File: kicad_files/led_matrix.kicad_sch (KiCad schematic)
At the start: 56 parts

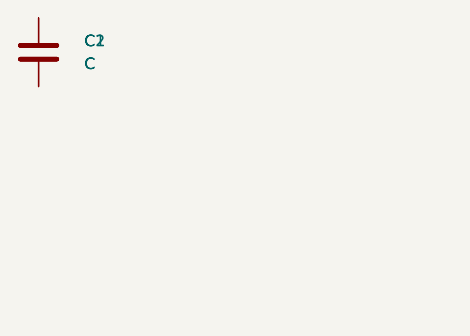
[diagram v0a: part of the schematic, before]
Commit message: Added footprints
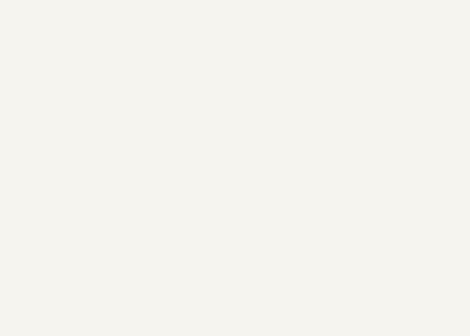
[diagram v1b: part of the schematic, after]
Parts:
- removed C1, C2: C, symbol Device:C
- C10, C11, C12, C13, C14, C15, C16, C17, C18, C19, C20, C21, C22, C23, C24, C25, C26, C27, C28, C29, C3, C4, C5, C6, C7, C8, C9: footprint (none) -> Capacitor_SMD:C_0603_1608Metric_Pad1.08x0.95mm_HandSolder
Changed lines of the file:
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@@
 			)
 		)
-		(property "Footprint" ""
+		(property "Footprint" "Capacitor_SMD:C_0603_1608Metric_Pad1.08x0.95mm_HandSolder"
 			(at 143.8402 88.9 0)
 			(hide yes)
@@
 	)
 	(symbol
-		(lib_id "Device:C")
-		(at -116.84 -19.685 0)
-		(unit 1)
-		(body_style 1)
-		(exclude_from_sim no)
-		(in_bom yes)
-		(on_board yes)
-		(in_pos_files yes)
-		(dnp no)
-		(fields_autoplaced yes)
-		(property "Reference" "C1"
-			(at -111.76 -20.9551 0)
-			(show_name no)
-			(do_not_autoplace no)
-			(effects
-				(font
-					(size 1.27 1.27)
-				)
-				(justify left)
-			)
-		)
-		(property "Value" "C"
-			(at -111.76 -18.4151 0)
-			(show_name no)
-			(do_not_autoplace no)
-			(effects
-				(font
-					(size 1.27 1.27)
-				)
-				(justify left)
-			)
-		)
-		(property "Footprint" ""
-			(at -115.8748 -15.875 0)
-			(hide yes)
-			(show_name no)
-			(do_not_autoplace no)
-			(effects
-				(font
-					(size 1.27 1.27)
-				)
-			)
-		)
-		(property "Datasheet" ""
-			(at -116.84 -19.685 0)
-			(hide yes)
-			(show_name no)
-			(do_not_autoplace no)
-			(effects
-				(font
-					(size 1.27 1.27)
-				)
-			)
-		)
-		(property "Description" "Unpolarized capacitor"
-			(at -116.84 -19.685 0)
-			(hide yes)
-			(show_name no)
-			(do_not_autoplace no)
-			(effects
-				(font
-					(size 1.27 1.27)
-				)
-			)
-		)
-		(pin "1"
-		)
-		(pin "2"
-		)
-		(instances
-			(project "keeb"
-				(path "/616400a8-c028-4d1b-bedc-b9aa63c43c10/898cb191-e761-44e4-85cc-feb2b69be915"
-					(reference "C1")
-					(unit 1)
-				)
-			)
-		)
-	)
-	(symbol
 		(lib_id "LED:SK6812MINI-E")
 		(at 208.28 88.9 0)
@@
 			)
 		)
-		(property "Footprint" ""
+		(property "Footprint" "Capacitor_SMD:C_0603_1608Metric_Pad1.08x0.95mm_HandSolder"
 			(at 143.8402 120.65 0)
 			(hide yes)
@@
 			)
 		)
-		(property "Footprint" ""
+		(property "Footprint" "Capacitor_SMD:C_0603_1608Metric_Pad1.08x0.95mm_HandSolder"
 			(at 100.0252 59.69 0)
 			(hide yes)
@@
 			)
 		)
-		(property "Footprint" ""
+		(property "Footprint" "Capacitor_SMD:C_0603_1608Metric_Pad1.08x0.95mm_HandSolder"
 			(at 100.0252 120.65 0)
 			(hide yes)
@@
 			)
 		)
-		(property "Footprint" ""
+		(property "Footprint" "Capacitor_SMD:C_0603_1608Metric_Pad1.08x0.95mm_HandSolder"
 			(at 188.9252 59.69 0)
 			(hide yes)
@@
 			)
 		)
-		(property "Footprint" ""
+		(property "Footprint" "Capacitor_SMD:C_0603_1608Metric_Pad1.08x0.95mm_HandSolder"
 			(at 143.8402 59.69 0)
 			(hide yes)
@@
 			)
 		)
-		(property "Footprint" ""
+		(property "Footprint" "Capacitor_SMD:C_0603_1608Metric_Pad1.08x0.95mm_HandSolder"
 			(at 53.6702 150.495 0)
 			(hide yes)
@@
 			)
 		)
-		(property "Footprint" ""
+		(property "Footprint" "Capacitor_SMD:C_0603_1608Metric_Pad1.08x0.95mm_HandSolder"
 			(at 100.0252 150.495 0)
 			(hide yes)
@@
 			)
 		)
-		(property "Footprint" ""
+		(property "Footprint" "Capacitor_SMD:C_0603_1608Metric_Pad1.08x0.95mm_HandSolder"
 			(at 188.9252 120.65 0)
 			(hide yes)
@@
 			)
 		)
-		(property "Footprint" ""
+		(property "Footprint" "Capacitor_SMD:C_0603_1608Metric_Pad1.08x0.95mm_HandSolder"
 			(at 100.6602 88.9 0)
 			(hide yes)
@@
 			)
 		)
-		(property "Footprint" ""
+		(property "Footprint" "Capacitor_SMD:C_0603_1608Metric_Pad1.08x0.95mm_HandSolder"
 			(at 188.9252 88.9 0)
 			(hide yes)
@@
 			)
 		)
-		(property "Footprint" ""
+		(property "Footprint" "Capacitor_SMD:C_0603_1608Metric_Pad1.08x0.95mm_HandSolder"
 			(at 277.8252 150.495 0)
 			(hide yes)
@@
 			)
 		)
-		(property "Footprint" ""
+		(property "Footprint" "Capacitor_SMD:C_0603_1608Metric_Pad1.08x0.95mm_HandSolder"
 			(at 53.6702 179.07 0)
 			(hide yes)
@@
 			)
 		)
-		(property "Footprint" ""
+		(property "Footprint" "Capacitor_SMD:C_0603_1608Metric_Pad1.08x0.95mm_HandSolder"
 			(at 232.7402 88.9 0)
 			(hide yes)
@@
 			)
 		)
-		(property "Footprint" ""
+		(property "Footprint" "Capacitor_SMD:C_0603_1608Metric_Pad1.08x0.95mm_HandSolder"
 			(at 277.8252 88.9 0)
 			(hide yes)
@@
 			)
 		)
-		(property "Footprint" ""
+		(property "Footprint" "Capacitor_SMD:C_0603_1608Metric_Pad1.08x0.95mm_HandSolder"
 			(at 143.8402 179.07 0)
 			(hide yes)
@@
 			)
 		)
-		(property "Footprint" ""
+		(property "Footprint" "Capacitor_SMD:C_0603_1608Metric_Pad1.08x0.95mm_HandSolder"
 			(at 143.8402 150.495 0)
 			(hide yes)
@@
 			)
 		)
-		(property "Footprint" ""
+		(property "Footprint" "Capacitor_SMD:C_0603_1608Metric_Pad1.08x0.95mm_HandSolder"
 			(at 232.7402 59.69 0)
 			(hide yes)
@@
 			)
 		)
-		(property "Footprint" ""
+		(property "Footprint" "Capacitor_SMD:C_0603_1608Metric_Pad1.08x0.95mm_HandSolder"
 			(at 54.3052 120.65 0)
 			(hide yes)
@@
 			)
 		)
-		(property "Footprint" ""
+		(property "Footprint" "Capacitor_SMD:C_0603_1608Metric_Pad1.08x0.95mm_HandSolder"
 			(at 100.0252 179.07 0)
 			(hide yes)
@@
 			)
 		)
-		(property "Footprint" ""
+		(property "Footprint" "Capacitor_SMD:C_0603_1608Metric_Pad1.08x0.95mm_HandSolder"
 			(at 277.8252 120.65 0)
 			(hide yes)
@@
 			)
 		)
-		(property "Footprint" ""
+		(property "Footprint" "Capacitor_SMD:C_0603_1608Metric_Pad1.08x0.95mm_HandSolder"
 			(at 54.3052 88.9 0)
 			(hide yes)
@@
 	)
 	(symbol
-		(lib_id "Device:C")
-		(at -116.84 -19.685 0)
-		(unit 1)
-		(body_style 1)
-		(exclude_from_sim no)
-		(in_bom yes)
-		(on_board yes)
-		(in_pos_files yes)
-		(dnp no)
-		(fields_autoplaced yes)
-		(property "Reference" "C2"
-			(at -111.76 -20.9551 0)
-			(show_name no)
-			(do_not_autoplace no)
-			(effects
-				(font
-					(size 1.27 1.27)
-				)
-				(justify left)
-			)
-		)
-		(property "Value" "C"
-			(at -111.76 -18.4151 0)
-			(show_name no)
-			(do_not_autoplace no)
-			(effects
-				(font
-					(size 1.27 1.27)
-				)
-				(justify left)
-			)
-		)
-		(property "Footprint" ""
-			(at -115.8748 -15.875 0)
-			(hide yes)
-			(show_name no)
-			(do_not_autoplace no)
-			(effects
-				(font
-					(size 1.27 1.27)
-				)
-			)
-		)
-		(property "Datasheet" ""
-			(at -116.84 -19.685 0)
-			(hide yes)
-			(show_name no)
-			(do_not_autoplace no)
-			(effects
-				(font
-					(size 1.27 1.27)
-				)
-			)
-		)
-		(property "Description" "Unpolarized capacitor"
-			(at -116.84 -19.685 0)
-			(hide yes)
-			(show_name no)
-			(do_not_autoplace no)
-			(effects
-				(font
-					(size 1.27 1.27)
-				)
-			)
-		)
-		(pin "1"
-		)
-		(pin "2"
-		)
-		(instances
-			(project "keeb"
-				(path "/616400a8-c028-4d1b-bedc-b9aa63c43c10/898cb191-e761-44e4-85cc-feb2b69be915"
-					(reference "C2")
-					(unit 1)
-				)
-			)
-		)
-	)
-	(symbol
 		(lib_id "power:GND")
 		(at 231.775 62.865 0)
@@
 			)
 		)
-		(property "Footprint" ""
+		(property "Footprint" "Capacitor_SMD:C_0603_1608Metric_Pad1.08x0.95mm_HandSolder"
 			(at 188.9252 150.495 0)
 			(hide yes)
@@
 			)
 		)
-		(property "Footprint" ""
+		(property "Footprint" "Capacitor_SMD:C_0603_1608Metric_Pad1.08x0.95mm_HandSolder"
 			(at 232.7402 120.65 0)
 			(hide yes)
@@
 			)
 		)
-		(property "Footprint" ""
+		(property "Footprint" "Capacitor_SMD:C_0603_1608Metric_Pad1.08x0.95mm_HandSolder"
 			(at 54.3052 59.69 0)
 			(hide yes)
@@
 			)
 		)
-		(property "Footprint" ""
+		(property "Footprint" "Capacitor_SMD:C_0603_1608Metric_Pad1.08x0.95mm_HandSolder"
 			(at 277.8252 59.69 0)
 			(hide yes)
@@
 			)
 		)
-		(property "Footprint" ""
+		(property "Footprint" "Capacitor_SMD:C_0603_1608Metric_Pad1.08x0.95mm_HandSolder"
 			(at 232.7402 150.495 0)
 			(hide yes)
